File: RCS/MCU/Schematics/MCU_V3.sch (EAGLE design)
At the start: 26 parts, among them IC1 FT232RL, Q1 8 MHz, U1 ATMEGA328P_TQFP, X1 USB-A

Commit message: Started working on PCB
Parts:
- removed Q1: 8 MHz, adafruit:CRYSTALHC33U-V
- added Q2: 8 MHz, adafruit:CRYSTALHC49S
- LED4: value Blue -> Green; device adafruit:LED5MM -> adafruit:LED
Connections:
- net N$2: now also Q2.2; no longer Q1.2
- net N$3: now also Q2.1; no longer Q1.1
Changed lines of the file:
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@@
 <part name="SUPPLY1" library="SparkFun-Aesthetics" deviceset="VDD" device="" value="3.3 V"/>
 <part name="R1" library="resistor" deviceset="R-US_" device="R0805" value="10k"/>
-<part name="Q1" library="adafruit" deviceset="CRYSTAL" device="HC33U-V" value="8 MHz"/>
 <part name="C1" library="capacitor-wima" deviceset="C" device="2,5-3" value="22 pF"/>
 <part name="C2" library="capacitor-wima" deviceset="C" device="2,5-3" value="22 pF"/>
@@
 <part name="R5" library="resistor" deviceset="R-US_" device="R0805" value="100"/>
 <part name="R6" library="resistor" deviceset="R-US_" device="R0805" value="100"/>
-<part name="LED4" library="adafruit" deviceset="LED" device="5MM" value="Blue"/>
 <part name="R7" library="resistor" deviceset="R-US_" device="R0805" value="100"/>
 <part name="GND11" library="supply1" deviceset="GND" device=""/>
@@
 <part name="C6" library="capacitor-wima" deviceset="C" device="2,5-3" value="0.1 uF"/>
 <part name="GND12" library="supply1" deviceset="GND" device=""/>
+<part name="LED4" library="adafruit" deviceset="LED" device="" value="Green"/>
+<part name="Q2" library="adafruit" deviceset="CRYSTAL" device="HC49S" value="8 MHz"/>
 </parts>
 <sheets>
@@
 <instance part="SUPPLY1" gate="VDD" x="20.32" y="104.14"/>
 <instance part="R1" gate="G$1" x="20.32" y="81.28" rot="R90"/>
-<instance part="Q1" gate="G$1" x="17.78" y="45.72" rot="R90"/>
 <instance part="C1" gate="G$1" x="7.62" y="40.64" rot="R90"/>
 <instance part="C2" gate="G$1" x="7.62" y="50.8" rot="R90"/>
@@
 <instance part="R5" gate="G$1" x="162.56" y="22.86" rot="R90"/>
 <instance part="R6" gate="G$1" x="172.72" y="22.86" rot="R90"/>
-<instance part="LED4" gate="G$1" x="91.44" y="33.02"/>
 <instance part="R7" gate="G$1" x="91.44" y="20.32" rot="R90"/>
 <instance part="GND11" gate="1" x="91.44" y="10.16"/>
@@
 <instance part="C6" gate="G$1" x="-7.62" y="60.96"/>
 <instance part="GND12" gate="1" x="-12.7" y="48.26"/>
+<instance part="LED4" gate="G$1" x="91.44" y="33.02"/>
+<instance part="Q2" gate="G$1" x="17.78" y="45.72" rot="R90"/>
 </instances>
 <busses>
@@
 <net name="N$2" class="0">
 <segment>
-<pinref part="Q1" gate="G$1" pin="2"/>
 <wire x1="35.56" y1="48.26" x2="17.78" y2="48.26" width="0.1524" layer="91"/>
 <pinref part="C2" gate="G$1" pin="2"/>
 <wire x1="17.78" y1="48.26" x2="17.78" y2="50.8" width="0.1524" layer="91"/>
 <wire x1="17.78" y1="50.8" x2="12.7" y2="50.8" width="0.1524" layer="91"/>
+<pinref part="U1" gate="U$1" pin="PB6(XTAL1/TOSC1)"/>
+<pinref part="Q2" gate="G$1" pin="2"/>
 <junction x="17.78" y="48.26"/>
-<pinref part="U1" gate="U$1" pin="PB6(XTAL1/TOSC1)"/>
 </segment>
 </net>
 <net name="N$3" class="0">
 <segment>
-<pinref part="Q1" gate="G$1" pin="1"/>
 <wire x1="35.56" y1="43.18" x2="17.78" y2="43.18" width="0.1524" layer="91"/>
 <pinref part="C1" gate="G$1" pin="2"/>
 <wire x1="17.78" y1="43.18" x2="17.78" y2="40.64" width="0.1524" layer="91"/>
 <wire x1="17.78" y1="40.64" x2="12.7" y2="40.64" width="0.1524" layer="91"/>
+<pinref part="U1" gate="U$1" pin="PB7(XTAL2/TOSC2)"/>
+<pinref part="Q2" gate="G$1" pin="1"/>
 <junction x="17.78" y="43.18"/>
-<pinref part="U1" gate="U$1" pin="PB7(XTAL2/TOSC2)"/>
 </segment>
 </net>
@@
 <segment>
 <pinref part="U1" gate="U$1" pin="PD3(INT1)"/>
-<pinref part="LED4" gate="G$1" pin="A"/>
 <wire x1="83.82" y1="43.18" x2="91.44" y2="43.18" width="0.1524" layer="91"/>
 <wire x1="91.44" y1="43.18" x2="91.44" y2="35.56" width="0.1524" layer="91"/>
-</segment>
-</net>
+<pinref part="LED4" gate="G$1" pin="A"/>
+</segment>
+</net>

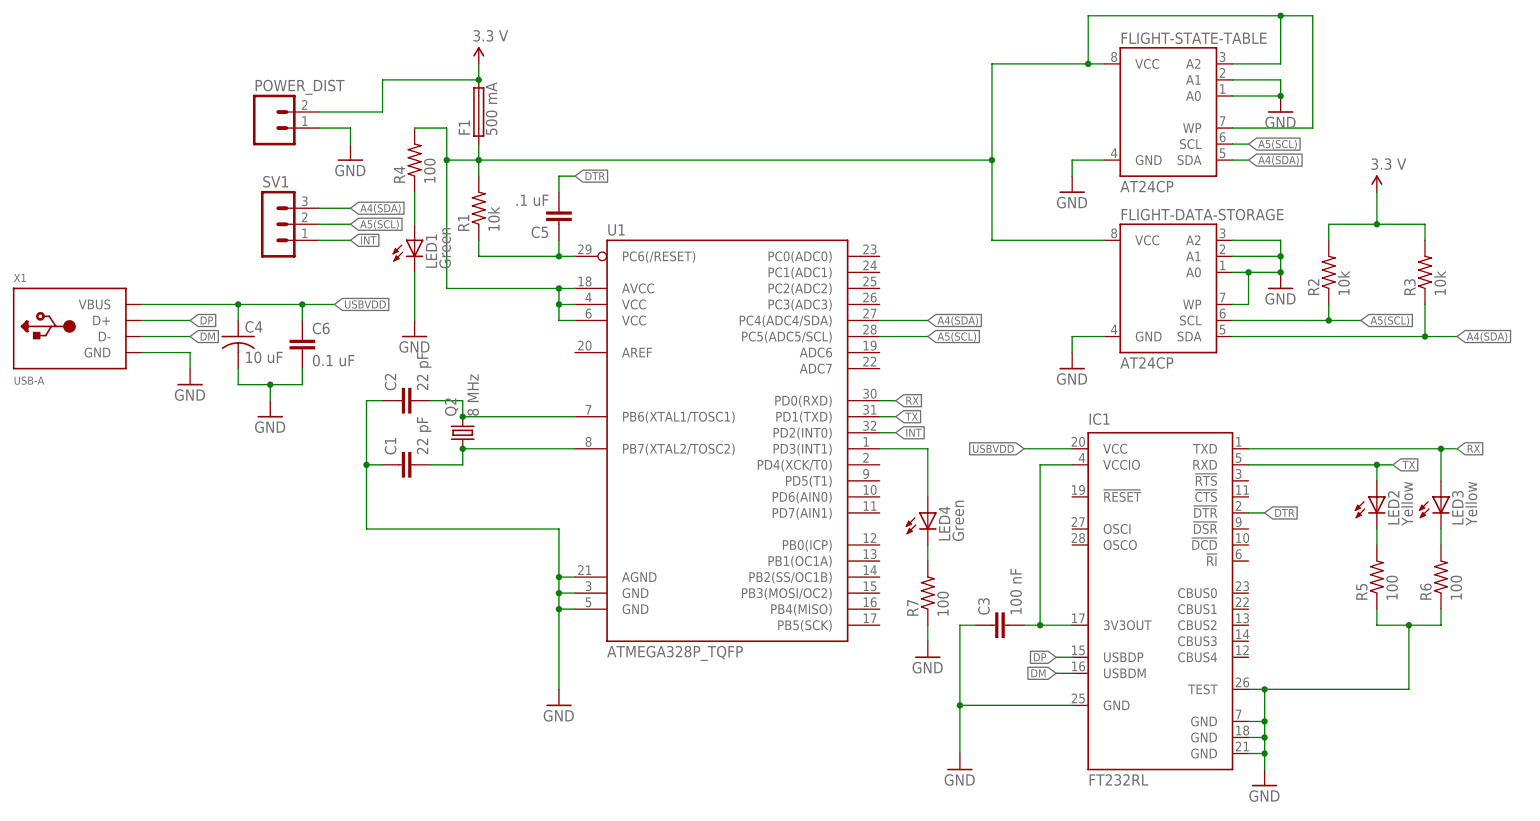
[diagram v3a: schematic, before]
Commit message: Completed PCB layout
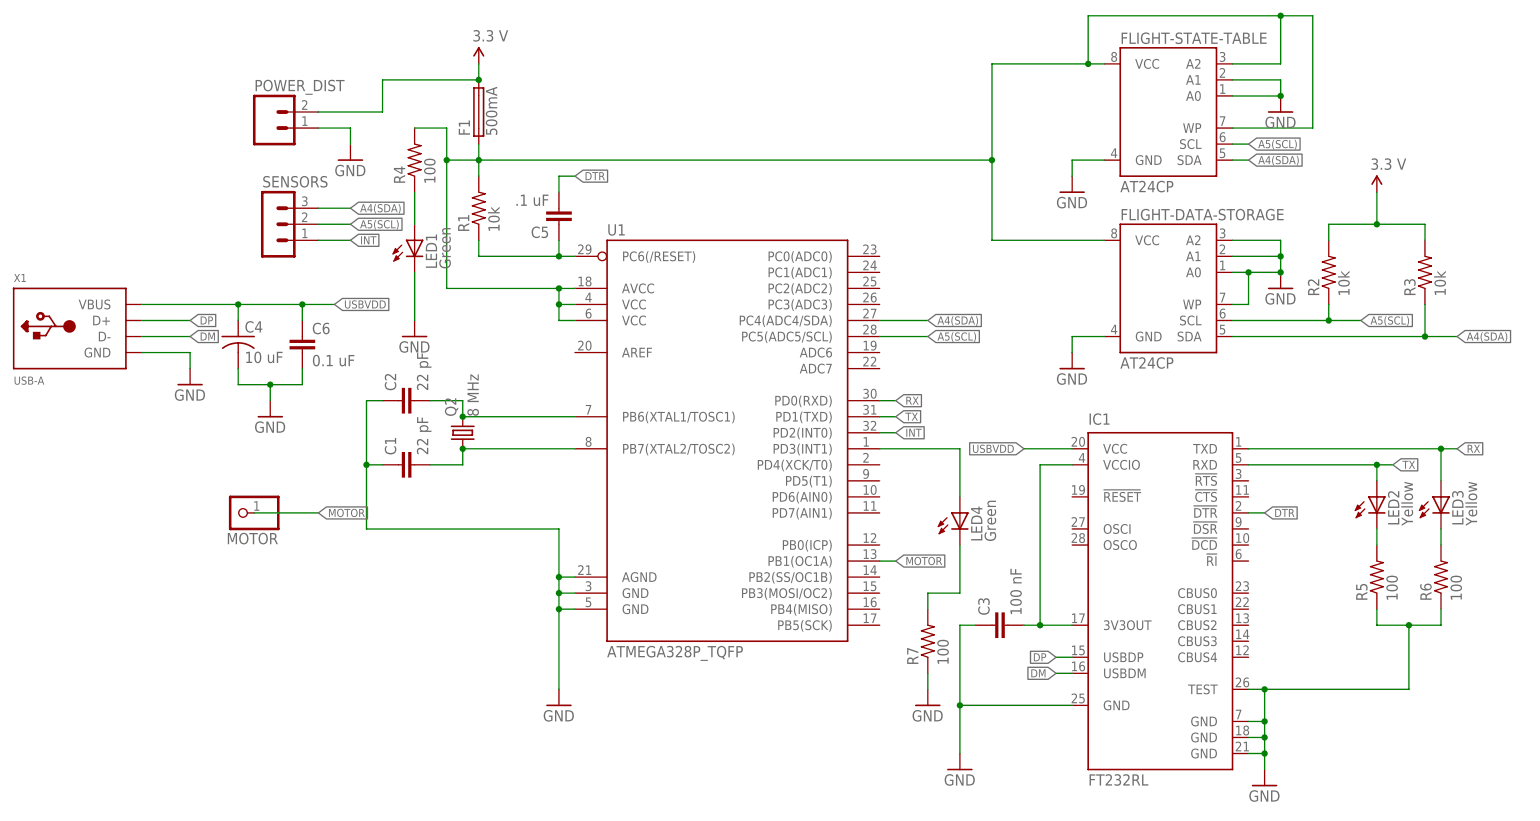
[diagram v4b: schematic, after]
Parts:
- added MOTOR: (no value), adafruit:PINHD-1X1
- F1: value 500 mA -> 500mA; device fuse:19559 -> fuse:PICOFUSE
- LED1, LED2, LED3, LED4: device adafruit:LED -> eagle-ltspice:LED_ESML0603
- renumbered SV1 to SENSORS
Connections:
- new net MOTOR: MOTOR.1, U1.PB1(OC1A)
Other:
- moved on the sheet: LED4, R7
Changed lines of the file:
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@@
 <part name="C2" library="capacitor-wima" deviceset="C" device="2,5-3" value="22 pF"/>
 <part name="GND1" library="supply1" deviceset="GND" device=""/>
-<part name="F1" library="fuse" deviceset="19559" device="" value="500 mA"/>
 <part name="FLIGHT-STATE-TABLE" library="atmel" deviceset="AT24C*" device="P"/>
 <part name="FLIGHT-DATA-STORAGE" library="atmel" deviceset="AT24C*" device="P"/>
@@
 <part name="GND9" library="supply1" deviceset="GND" device=""/>
 <part name="U1" library="SparkFun-DigitalIC" deviceset="ATMEGA328P_TQFP" device="" value="ATMEGA328P_TQFP"/>
-<part name="SV1" library="con-lstb" deviceset="MA03-1" device=""/>
-<part name="LED1" library="adafruit" deviceset="LED" device="" value="Green"/>
+<part name="SENSORS" library="con-lstb" deviceset="MA03-1" device=""/>
+<part name="LED1" library="eagle-ltspice" deviceset="LED_E" device="SML0603" value="Green"/>
 <part name="GND10" library="supply1" deviceset="GND" device=""/>
-<part name="LED2" library="adafruit" deviceset="LED" device="" value="Yellow"/>
-<part name="LED3" library="adafruit" deviceset="LED" device="" value="Yellow"/>
+<part name="LED2" library="eagle-ltspice" deviceset="LED_E" device="SML0603" value="Yellow"/>
+<part name="LED3" library="eagle-ltspice" deviceset="LED_E" device="SML0603" value="Yellow"/>
 <part name="R4" library="resistor" deviceset="R-US_" device="R0805" value="100"/>
 <part name="R5" library="resistor" deviceset="R-US_" device="R0805" value="100"/>
@@
 <part name="C6" library="capacitor-wima" deviceset="C" device="2,5-3" value="0.1 uF"/>
 <part name="GND12" library="supply1" deviceset="GND" device=""/>
-<part name="LED4" library="adafruit" deviceset="LED" device="" value="Green"/>
+<part name="LED4" library="eagle-ltspice" deviceset="LED_E" device="SML0603" value="Green"/>
 <part name="Q2" library="adafruit" deviceset="CRYSTAL" device="HC49S" value="8 MHz"/>
+<part name="MOTOR" library="adafruit" deviceset="PINHD-1X1" device=""/>
+<part name="F1" library="fuse" deviceset="PICOFUSE" device="" value="500mA"/>
 </parts>
 <sheets>
@@
 <instance part="C2" gate="G$1" x="7.62" y="50.8" rot="R90"/>
 <instance part="GND1" gate="1" x="33.02" y="2.54"/>
-<instance part="F1" gate="1" x="20.32" y="96.52" rot="R90"/>
 <instance part="FLIGHT-STATE-TABLE" gate="G$1" x="129.54" y="96.52"/>
 <instance part="FLIGHT-DATA-STORAGE" gate="G$1" x="129.54" y="68.58"/>
@@
 <instance part="GND9" gate="1" x="147.32" y="96.52"/>
 <instance part="U1" gate="U$1" x="60.96" y="43.18"/>
-<instance part="SV1" gate="G$1" x="-12.7" y="78.74"/>
+<instance part="SENSORS" gate="G$1" x="-12.7" y="78.74"/>
 <instance part="LED1" gate="G$1" x="10.16" y="76.2"/>
 <instance part="GND10" gate="1" x="10.16" y="60.96"/>
@@
 <instance part="R5" gate="G$1" x="162.56" y="22.86" rot="R90"/>
 <instance part="R6" gate="G$1" x="172.72" y="22.86" rot="R90"/>
-<instance part="R7" gate="G$1" x="91.44" y="20.32" rot="R90"/>
-<instance part="GND11" gate="1" x="91.44" y="10.16"/>
+<instance part="R7" gate="G$1" x="91.44" y="12.7" rot="R90"/>
+<instance part="GND11" gate="1" x="91.44" y="2.54"/>
 <instance part="C4" gate="G$1" x="-17.78" y="60.96"/>
 <instance part="C6" gate="G$1" x="-7.62" y="60.96"/>
 <instance part="GND12" gate="1" x="-12.7" y="48.26"/>
-<instance part="LED4" gate="G$1" x="91.44" y="33.02"/>
+<instance part="LED4" gate="G$1" x="96.52" y="33.02"/>
 <instance part="Q2" gate="G$1" x="17.78" y="45.72" rot="R90"/>
+<instance part="MOTOR" gate="G$1" x="-17.78" y="33.02" rot="R180"/>
+<instance part="F1" gate="1" x="20.32" y="96.52" rot="R90"/>
 </instances>
 <busses>
@@
 <pinref part="R7" gate="G$1" pin="1"/>
 <pinref part="GND11" gate="1" pin="GND"/>
-<wire x1="91.44" y1="15.24" x2="91.44" y2="12.7" width="0.1524" layer="91"/>
+<wire x1="91.44" y1="7.62" x2="91.44" y2="5.08" width="0.1524" layer="91"/>
 </segment>
 <segment>
@@
 <segment>
 <pinref part="SUPPLY1" gate="VDD" pin="VDD"/>
-<pinref part="F1" gate="1" pin="2"/>
 <wire x1="20.32" y1="104.14" x2="20.32" y2="101.6" width="0.1524" layer="91"/>
 <wire x1="5.08" y1="96.52" x2="5.08" y2="101.6" width="0.1524" layer="91"/>
 <wire x1="5.08" y1="101.6" x2="20.32" y2="101.6" width="0.1524" layer="91"/>
-<junction x="20.32" y="101.6"/>
 <pinref part="POWER_DIST" gate="G$1" pin="2"/>
 <wire x1="-5.08" y1="96.52" x2="5.08" y2="96.52" width="0.1524" layer="91"/>
+<pinref part="F1" gate="1" pin="2"/>
+<junction x="20.32" y="101.6"/>
 </segment>
 <segment>
@@
 <segment>
 <label x="0" y="81.28" size="1.27" layer="95" xref="yes"/>
-<pinref part="SV1" gate="G$1" pin="3"/>
+<pinref part="SENSORS" gate="G$1" pin="3"/>
 <wire x1="-5.08" y1="81.28" x2="0" y2="81.28" width="0.1524" layer="91"/>
 </segment>
@@
 <segment>
 <label x="0" y="78.74" size="1.27" layer="95" xref="yes"/>
-<pinref part="SV1" gate="G$1" pin="2"/>
+<pinref part="SENSORS" gate="G$1" pin="2"/>
 <wire x1="-5.08" y1="78.74" x2="0" y2="78.74" width="0.1524" layer="91"/>
 </segment>
@@
 </segment>
 <segment>
-<pinref part="SV1" gate="G$1" pin="1"/>
+<pinref part="SENSORS" gate="G$1" pin="1"/>
 <wire x1="-5.08" y1="76.2" x2="0" y2="76.2" width="0.1524" layer="91"/>
 <label x="0" y="76.2" size="1.27" layer="95" xref="yes"/>
@@
 <pinref part="R1" gate="G$1" pin="2"/>
 <wire x1="147.32" y1="111.76" x2="116.84" y2="111.76" width="0.1524" layer="91"/>
-<pinref part="F1" gate="1" pin="1"/>
 <wire x1="20.32" y1="86.36" x2="20.32" y2="88.9" width="0.1524" layer="91"/>
 <wire x1="20.32" y1="88.9" x2="20.32" y2="91.44" width="0.1524" layer="91"/>
@@
 <wire x1="15.24" y1="68.58" x2="33.02" y2="68.58" width="0.1524" layer="91"/>
 <junction x="33.02" y="68.58"/>
+<pinref part="F1" gate="1" pin="1"/>
 </segment>
 </net>
@@
 <segment>
 <pinref part="U1" gate="U$1" pin="PD3(INT1)"/>
-<wire x1="83.82" y1="43.18" x2="91.44" y2="43.18" width="0.1524" layer="91"/>
-<wire x1="91.44" y1="43.18" x2="91.44" y2="35.56" width="0.1524" layer="91"/>
+<wire x1="83.82" y1="43.18" x2="96.52" y2="43.18" width="0.1524" layer="91"/>
+<wire x1="96.52" y1="43.18" x2="96.52" y2="35.56" width="0.1524" layer="91"/>
 <pinref part="LED4" gate="G$1" pin="A"/>
 </segment>
 </net>
+<net name="MOTOR" class="0">
+<segment>
+<wire x1="-15.24" y1="33.02" x2="-5.08" y2="33.02" width="0.1524" layer="91"/>
+<pinref part="MOTOR" gate="G$1" pin="1"/>
+<label x="-5.08" y="33.02" size="1.27" layer="95" xref="yes"/>
+</segment>
+<segment>
+<pinref part="U1" gate="U$1" pin="PB1(OC1A)"/>
+<wire x1="83.82" y1="25.4" x2="86.36" y2="25.4" width="0.1524" layer="91"/>
+<label x="86.36" y="25.4" size="1.27" layer="95" xref="yes"/>
+</segment>
+</net>
 <net name="N$8" class="0">
 <segment>
+<pinref part="R7" gate="G$1" pin="2"/>
+<wire x1="91.44" y1="20.32" x2="91.44" y2="17.78" width="0.1524" layer="91"/>
 <pinref part="LED4" gate="G$1" pin="C"/>
-<pinref part="R7" gate="G$1" pin="2"/>
-<wire x1="91.44" y1="27.94" x2="91.44" y2="25.4" width="0.1524" layer="91"/>
-</segment>
-</net>
+<wire x1="91.44" y1="20.32" x2="96.52" y2="20.32" width="0.1524" layer="91"/>
+<wire x1="96.52" y1="20.32" x2="96.52" y2="27.94" width="0.1524" layer="91"/>
+</segment>
+</net>

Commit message: Slightly updated schematic
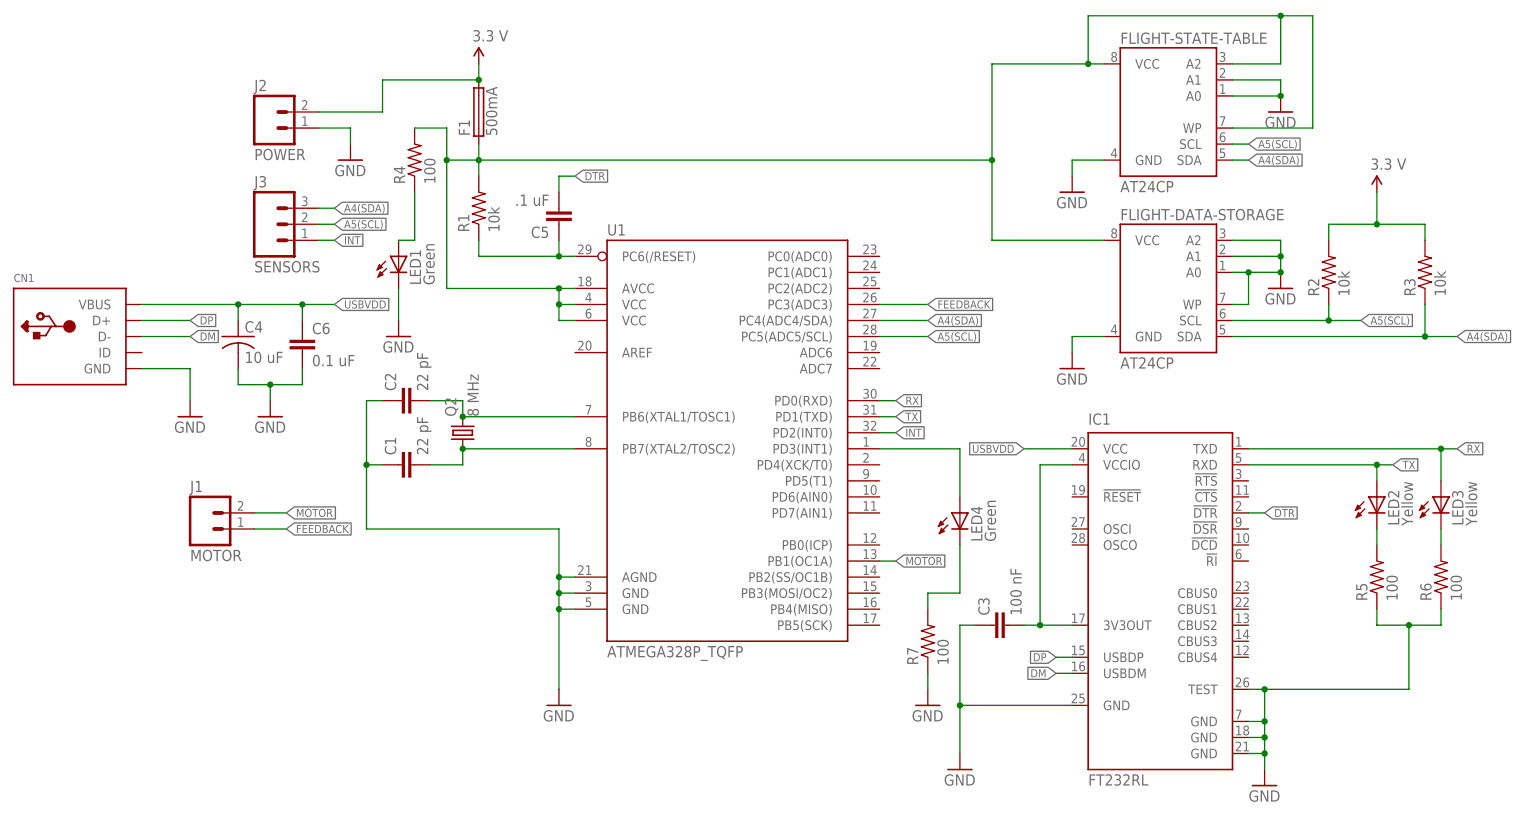
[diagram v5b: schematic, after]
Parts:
- removed MOTOR: (no value), adafruit:PINHD-1X1
- removed POWER_DIST: (no value), SparkFun-Connectors:M02PTH
- removed SENSORS: (no value), con-lstb:MA03-1
- removed X1: USB-A, adafruit:USB-A
- added CN1: (no value), adafruit:USBMOLEX
- added J1: MOTOR, SparkFun-Connectors:M02LOCK
- added J2: POWER, SparkFun-Connectors:M02LOCK
- added J3: SENSORS, SparkFun-Connectors:M03LOCK
- LED1, LED2, LED3, LED4: device eagle-ltspice:LED_ESML0603 -> adafruit:LEDCHIPLED_1206
- R1, R2, R3, R4, R5, R6, R7: device resistor:R-US_R0805 -> adafruit:R-US_R1206
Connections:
- new net FEEDBACK: J1.1, U1.PC3(ADC3)
- net A4(SDA): now also J3.3; no longer SENSORS.3
- net A5(SCL): now also J3.2; no longer SENSORS.2
- net DM: now also CN1.D-; no longer X1.D-
- net DP: now also CN1.D+; no longer X1.D+
- net GND: now also CN1.GND, J2.1; no longer POWER_DIST.1, X1.GND
- net INT: now also J3.1; no longer SENSORS.1
- net MOTOR: now also J1.2; no longer MOTOR.1
- net USBVDD: now also CN1.VBUS; no longer X1.VBUS
- net VDD: now also J2.2; no longer POWER_DIST.2
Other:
- moved on the sheet: LED1
